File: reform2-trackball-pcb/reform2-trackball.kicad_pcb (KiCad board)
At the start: 2 copper layers, 87.2 x 59 mm, 47 parts, among them J1 Conn_USB, J2 Conn_01x06_Female, SW1 Choc, SW2 Choc, SW3 Choc, SW4 Choc, SW5 Choc, SW6 SW_RST, SW7 SW_HWB, U1 ATmega32U2-AU, U2 TLV75533PDBV, U3 USBLC6-2SC6, Y1 Crystal_GND24

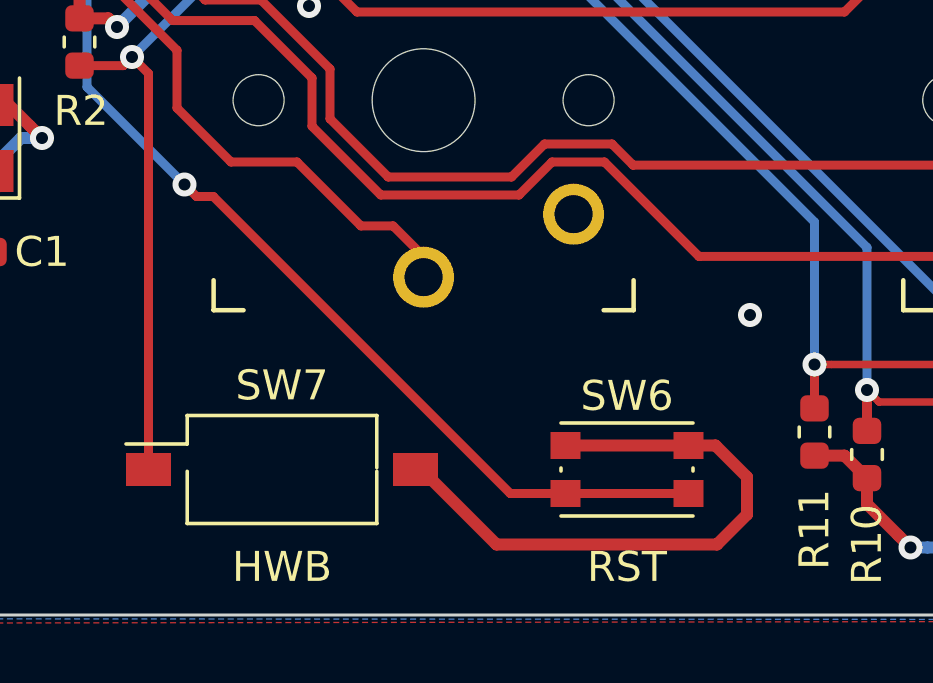
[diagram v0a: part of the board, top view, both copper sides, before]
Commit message: reform2: update PCBs incl. badges to production revs, add keyboard lettering, misc docs
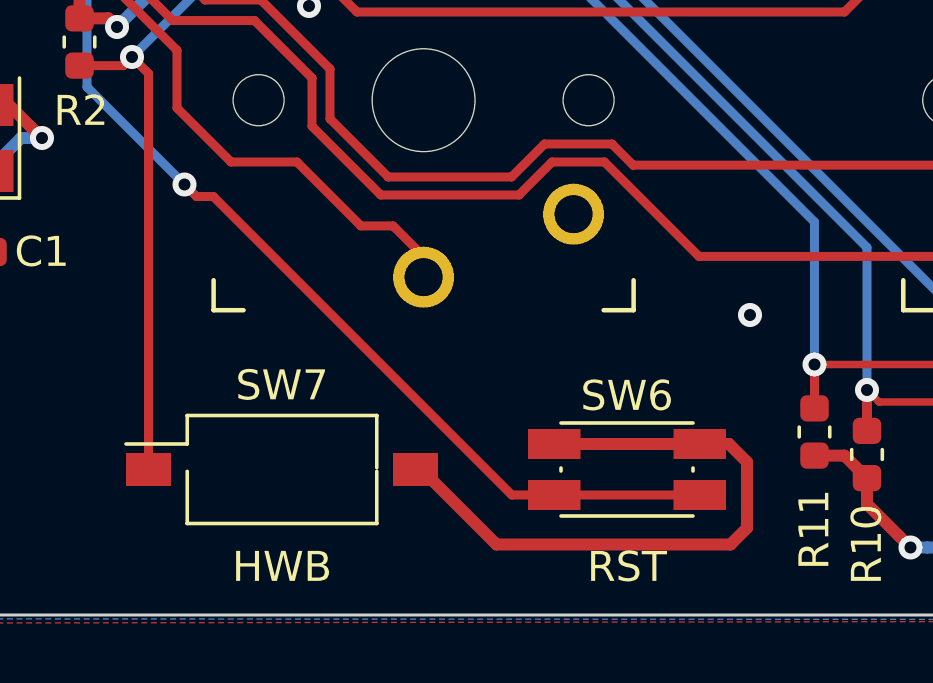
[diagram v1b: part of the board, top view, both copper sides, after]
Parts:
- SW6: footprint Button_Switch_SMD:SW_Push_1P1T_NO_CK_KMR2 -> footprints-trackball:Diptronics-PTLP2
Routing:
- net GND: track 61.5 -> 63.4 mm
